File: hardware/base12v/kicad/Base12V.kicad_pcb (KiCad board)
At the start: 2 copper layers, 50 x 60 mm, 18 parts, among them J1 ENTRADA 12V, J2 SALIDAS, J3 HC-05, J4 MODO, Q1 IRLZ44N, Q2 IRLZ44N, Q3 IRLZ44N

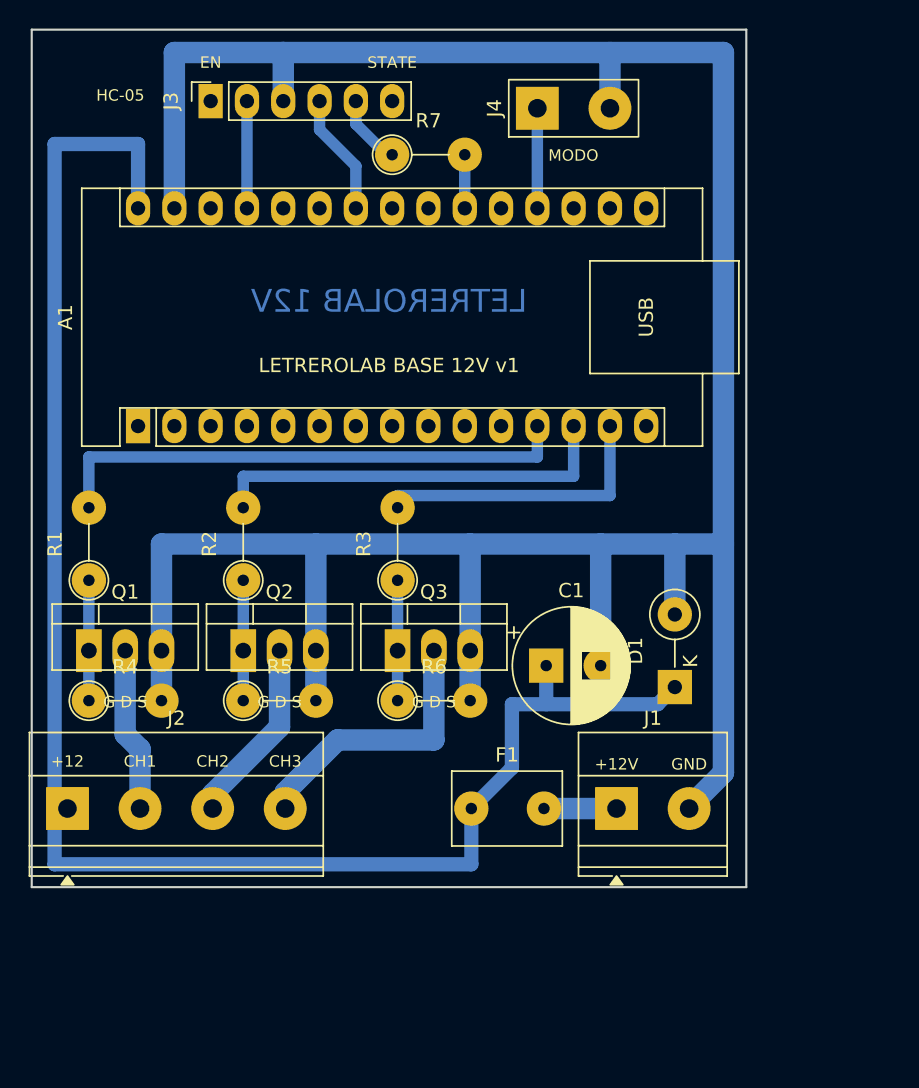
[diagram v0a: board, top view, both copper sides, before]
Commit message: Base board v1.1: M3 mounting holes, security enclosure, 3D models, JLCPCB package, roadmap
- Board grows to 60 x 72 mm with 4 M3 holes; ERC/DRC 0 with schematic parity.
- Component 3D models (KiCad 9.0.0 STEP + simple Arduino Nano VRML).
- Printable tamper-proof enclosure (gen/caja.py -> STL) with PG7 glands,
  security-screw lid and warranty-seal recess, plus a 1:1 template for metal boxes.
- Gerber zip ready for JLCPCB/PCBWay.
- HOJA_DE_RUTA.md: phases from home-made board to factory assembly.

Co-Authored-By: Claude Opus 5.5 <noreply@anthropic.com>
Claude-Session: https://claude.ai/code/session_01WVk3oGwfQfGTmAT2PMp8oW
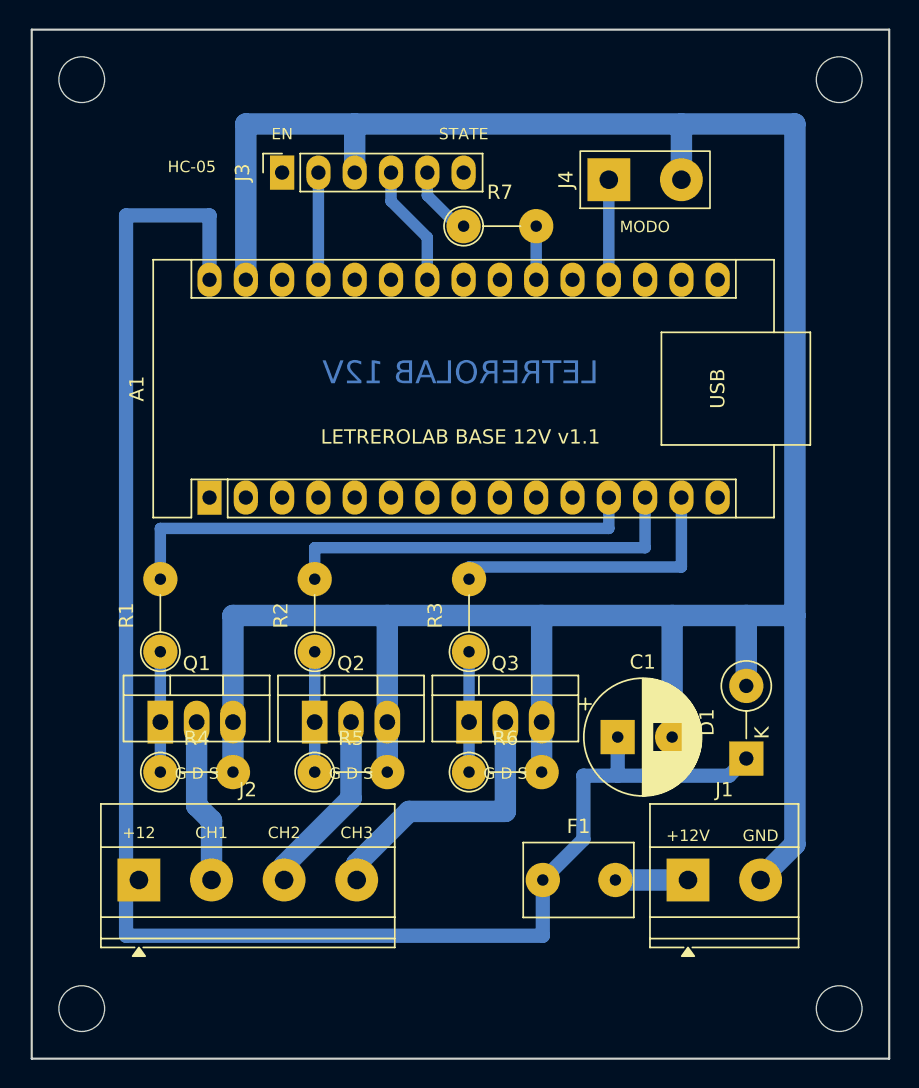
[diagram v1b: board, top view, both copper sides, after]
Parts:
- added H1: MountingHole_3.2mm_M3, Base12V:Barreno_M3_3.2mm, F.Cu at (103.5, 103.5)
- added H2: MountingHole_3.2mm_M3, Base12V:Barreno_M3_3.2mm, F.Cu at (156.5, 103.5)
- added H3: MountingHole_3.2mm_M3, Base12V:Barreno_M3_3.2mm, F.Cu at (103.5, 168.5)
- added H4: MountingHole_3.2mm_M3, Base12V:Barreno_M3_3.2mm, F.Cu at (156.5, 168.5)
- moved F1 7.07 mm to (135.8, 159.5)
- moved A1 7.07 mm to (112.4, 132.7)
- moved C1 7.07 mm to (141.0, 149.5)
- moved D1 7.07 mm to (150.0, 151.0)
- moved J1 7.07 mm to (145.9, 159.5)
- moved J2 7.07 mm to (107.5, 159.5)
- moved J3 7.07 mm to (117.5, 110.0)
- moved J4 7.07 mm to (140.4, 110.5)
- moved Q1 7.07 mm to (109.0, 148.4)
- moved Q2 7.07 mm to (119.8, 148.4)
- moved Q3 7.07 mm to (130.6, 148.4)
- moved R1 7.07 mm to (109.0, 143.5)
- moved R2 7.07 mm to (119.8, 143.5)
- moved R3 7.07 mm to (130.6, 143.5)
- moved R4 7.07 mm to (109.0, 151.9)
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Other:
- board size 50 x 60 mm -> 60 x 72 mm
- board text added: "LETREROLAB BASE 12V v1.1"
- board text removed: "LETREROLAB BASE 12V v1"
